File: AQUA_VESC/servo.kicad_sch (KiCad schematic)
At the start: 14 parts, among them M1 Motor_Servo_Hitec, U13 TP2604-SR

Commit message: AQUA VESC仮完成
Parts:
- removed C69: 1n, Capacitor_SMD:C_0603_1608Metric, symbol Device:C
- U11: renamed from U12; value ~ -> MX27524ES
- renumbered C67 to C65, C68 to C66, C70 to C67, R78 to R77, R79 to R78, R80 to R79, R81 to R80, R82 to R81, R83 to R82, R84 to R83, U13 to U12

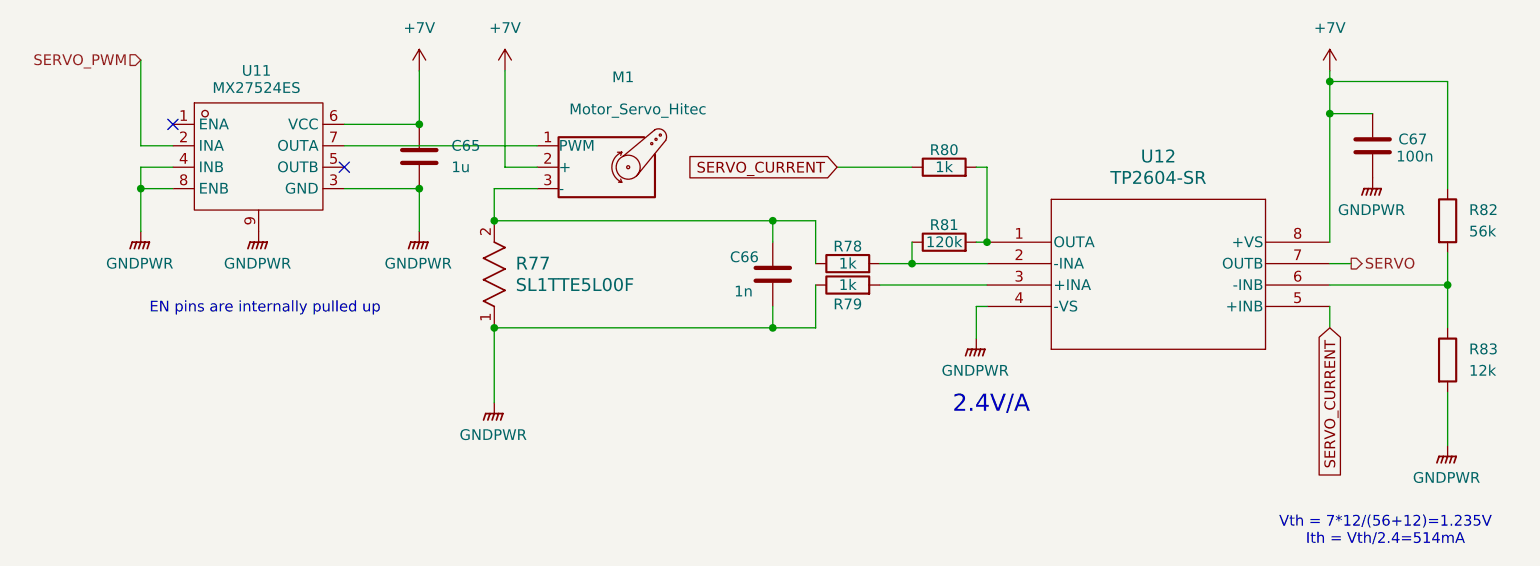
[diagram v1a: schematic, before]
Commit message: AQUA_VESC REV01作成
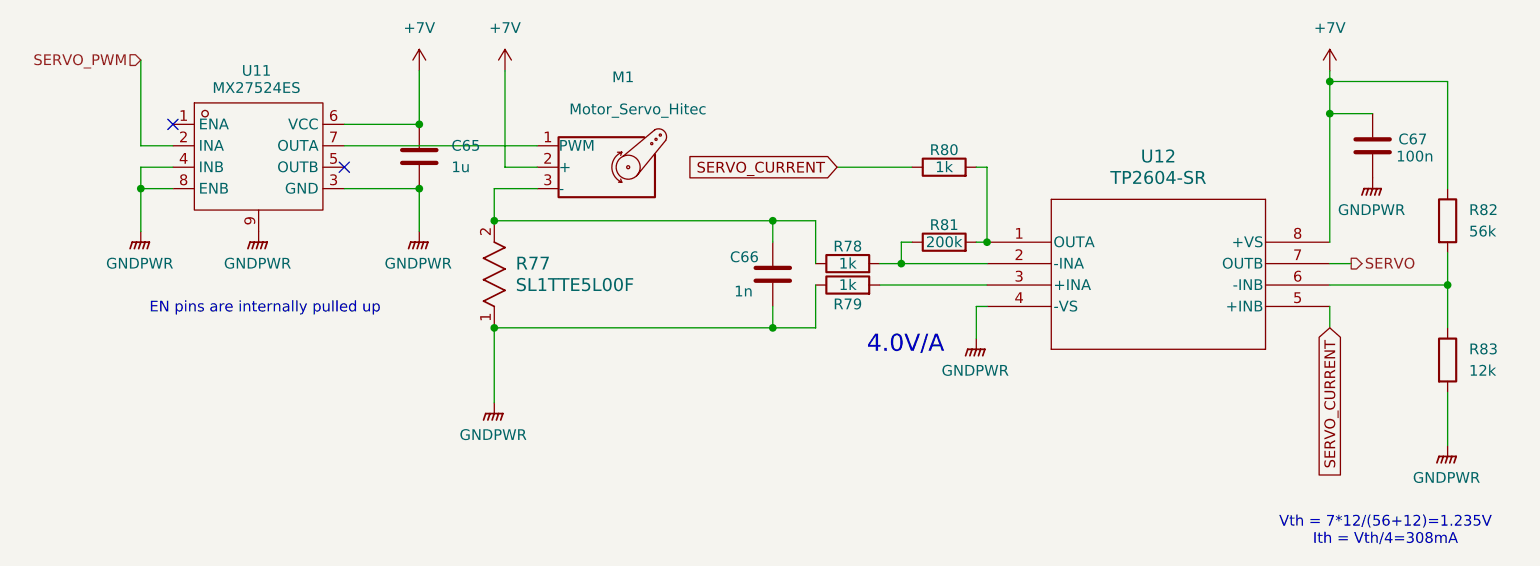
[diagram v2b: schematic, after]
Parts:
- R81: value 120k -> 200k
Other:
- note added: "4.0V/A"
- note added: "Vth = 7*12/(56+12)=1.235V Ith = Vth/4=308mA"
- note removed: "2.4V/A"
- note removed: "Vth = 7*12/(56+12)=1.235V Ith = Vth/2.4=514mA"
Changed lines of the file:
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@@
 		)
 	)
-	(text "2.4V/A"
+	(text "4.0V/A"
 		(exclude_from_sim no)
-		(at 127.508 78.994 0)
+		(at 117.348 71.882 0)
 		(effects
 			(font
@@
 		)
 	)
-	(text "Vth = 7*12/(56+12)=1.235V\nIth = Vth/2.4=514mA"
+	(text "Vth = 7*12/(56+12)=1.235V\nIth = Vth/4=308mA"
 		(exclude_from_sim no)
 		(at 174.244 93.98 0)
@@
 	)
 	(junction
-		(at 118.11 62.23)
+		(at 116.84 62.23)
 		(diameter 0)
 		(color 0 0 0 0)
@@
 	(wire
 		(pts
-			(xy 114.3 62.23) (xy 118.11 62.23)
+			(xy 114.3 62.23) (xy 116.84 62.23)
 		)
 		(stroke
@@
 	(wire
 		(pts
+			(xy 116.84 62.23) (xy 127 62.23)
+		)
+		(stroke
+			(width 0)
+			(type default)
+		)
+	)
+	(wire
+		(pts
 			(xy 114.3 64.77) (xy 127 64.77)
 		)
@@
 	(wire
 		(pts
+			(xy 116.84 59.69) (xy 118.11 59.69)
+		)
+		(stroke
+			(width 0)
+			(type default)
+		)
+	)
+	(wire
+		(pts
 			(xy 106.68 64.77) (xy 106.68 69.85)
 		)
@@
 	(wire
 		(pts
-			(xy 118.11 62.23) (xy 127 62.23)
-		)
-		(stroke
-			(width 0)
-			(type default)
-		)
-	)
-	(wire
-		(pts
 			(xy 181.61 64.77) (xy 181.61 60.96)
 		)
@@
 	(wire
 		(pts
-			(xy 118.11 59.69) (xy 118.11 62.23)
+			(xy 116.84 59.69) (xy 116.84 62.23)
 		)
 		(stroke
@@
 			)
 		)
-		(property "Value" "120k"
+		(property "Value" "200k"
 			(at 121.92 59.69 90)
 			(effects

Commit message: 制御基板REV01完成
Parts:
- removed C66: 1n, Capacitor_SMD:C_0603_1608Metric, symbol Device:C
- removed C67: 100n, Capacitor_SMD:C_0603_1608Metric, symbol Device:C
- removed R77: SL1TTE5L00F, specific_footprint_library:RES_SL1TTE5L00F_KOA, symbol specific_library:SL1TTE5L00F
- removed R78, R79, R80: 1k, Resistor_SMD:R_0603_1608Metric, symbol Device:R
- removed R81: 200k, Resistor_SMD:R_0603_1608Metric, symbol Device:R
- removed R82: 56k, Resistor_SMD:R_0603_1608Metric, symbol Device:R
- removed R83: 12k, Resistor_SMD:R_0603_1608Metric, symbol Device:R
- removed U12: TP2604-SR, specific_footprint_library:SO-8SOIC-8_TPK, symbol specific_library:TP2604-SR
- M1: footprint Connector_JST:JST_XA_S03B-XASK-1N-BN_1x03_P2.50mm_Horizontal -> Connector_PinSocket_2.54mm:PinSocket_1x03_P2.54mm_Horizontal
- renumbered C65 to C62, U11 to U9
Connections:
- net GNDPWR: now also M1.3 (-)
- net +7V renamed +6V
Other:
- note removed: "4.0V/A"
- note removed: "Vth = 7*12/(56+12)=1.235V Ith = Vth/4=308mA"
- moved on the sheet: C62, M1, U9
